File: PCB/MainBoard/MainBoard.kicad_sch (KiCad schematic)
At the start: 2 parts, among them J1 USB_C_Receptacle_USB2.0_14P

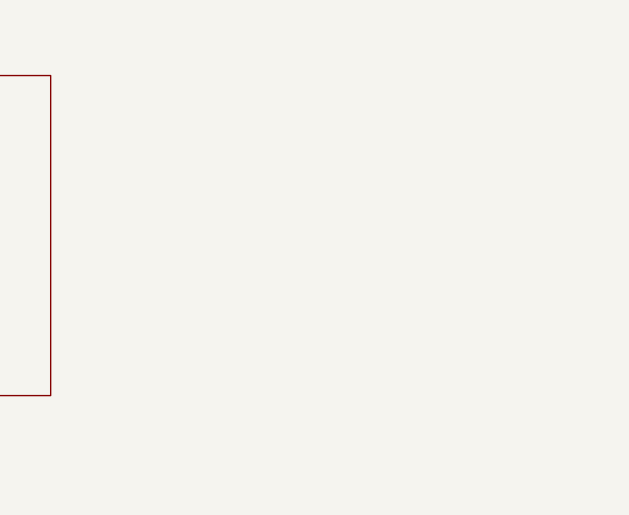
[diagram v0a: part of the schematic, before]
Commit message: Added IMU (just copied it tho...)
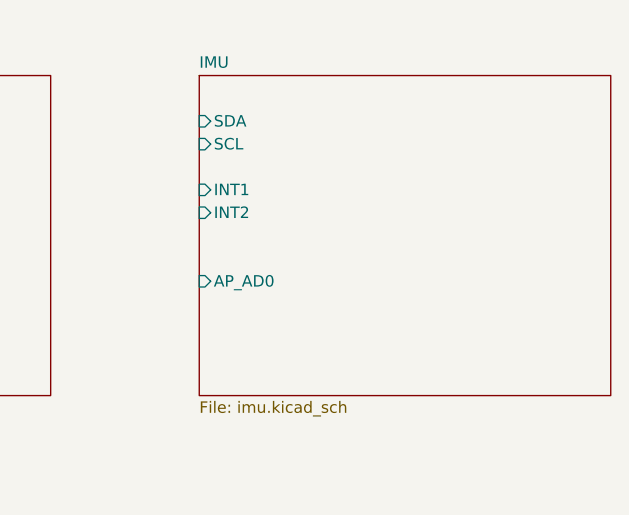
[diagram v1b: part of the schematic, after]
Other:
- added sheet IMU (imu.kicad_sch)
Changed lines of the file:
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@@
+	)
+	(sheet
+		(at 125.73 50.8)
+		(size 45.72 35.56)
+		(fields_autoplaced yes)
+		(stroke
+			(width 0.1524)
+			(type solid)
+		)
+		(fill
+			(color 0 0 0 0.0000)
+		)
+		(property "Sheetname" "IMU"
+			(at 125.73 50.0884 0)
+			(effects
+				(font
+					(size 1.27 1.27)
+				)
+				(justify left bottom)
+			)
+		)
+		(property "Sheetfile" "imu.kicad_sch"
+			(at 125.73 86.9446 0)
+			(effects
+				(font
+					(size 1.27 1.27)
+				)
+				(justify left top)
+			)
+		)
+		(pin "SDA" input
+			(at 125.73 55.88 180)
+			(effects
+				(font
+					(size 1.27 1.27)
+				)
+				(justify left)
+			)
+		)
+		(pin "SCL" input
+			(at 125.73 58.42 180)
+			(effects
+				(font
+					(size 1.27 1.27)
+				)
+				(justify left)
+			)
+		)
+		(pin "INT1" input
+			(at 125.73 63.5 180)
+			(effects
+				(font
+					(size 1.27 1.27)
+				)
+				(justify left)
+			)
+		)
+		(pin "AP_AD0" input
+			(at 125.73 73.66 180)
+			(effects
+				(font
+					(size 1.27 1.27)
+				)
+				(justify left)
+			)
+		)
+		(pin "INT2" input
+			(at 125.73 66.04 180)
+			(effects
+				(font
+					(size 1.27 1.27)
+				)
+				(justify left)
+			)
+		)
+		(instances
+			(project "MainBoard"
+				(path "/4b463b93-bd96-4cf6-bfe2-9d8869b16347"
+					(page "3")
+				)
+			)
+		)
 	)
 	(sheet

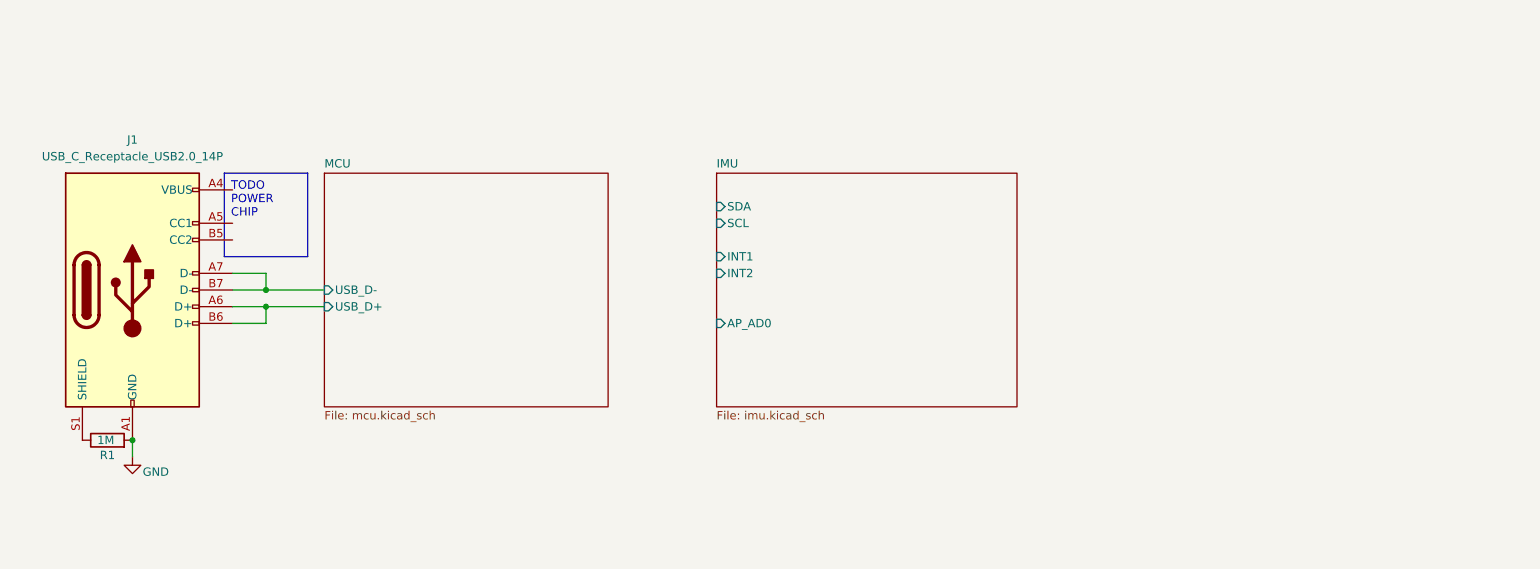
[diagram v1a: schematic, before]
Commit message: Repaired IMU and ESP symbols and footprints
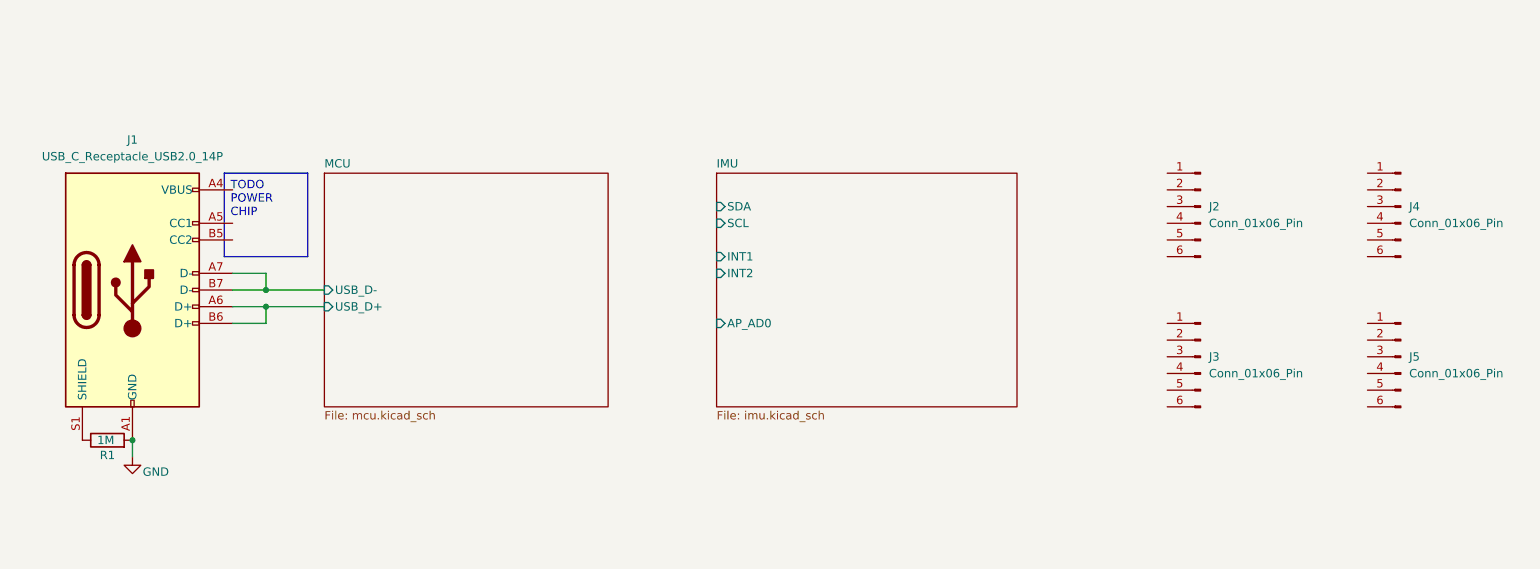
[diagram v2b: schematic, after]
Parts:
- added J2, J3, J4, J5: Conn_01x06_Pin, Connector_JST:JST_PH_B6B-PH-K_1x06_P2.00mm_Vertical, symbol Connector:Conn_01x06_Pin
- J1: footprint (none) -> Connector_USB:USB_C_Receptacle_HCTL_HC-TYPE-C-16P-01A
- R1: footprint (none) -> Resistor_SMD:R_0402_1005Metric_Pad0.72x0.64mm_HandSolder

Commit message: Added Buck converter
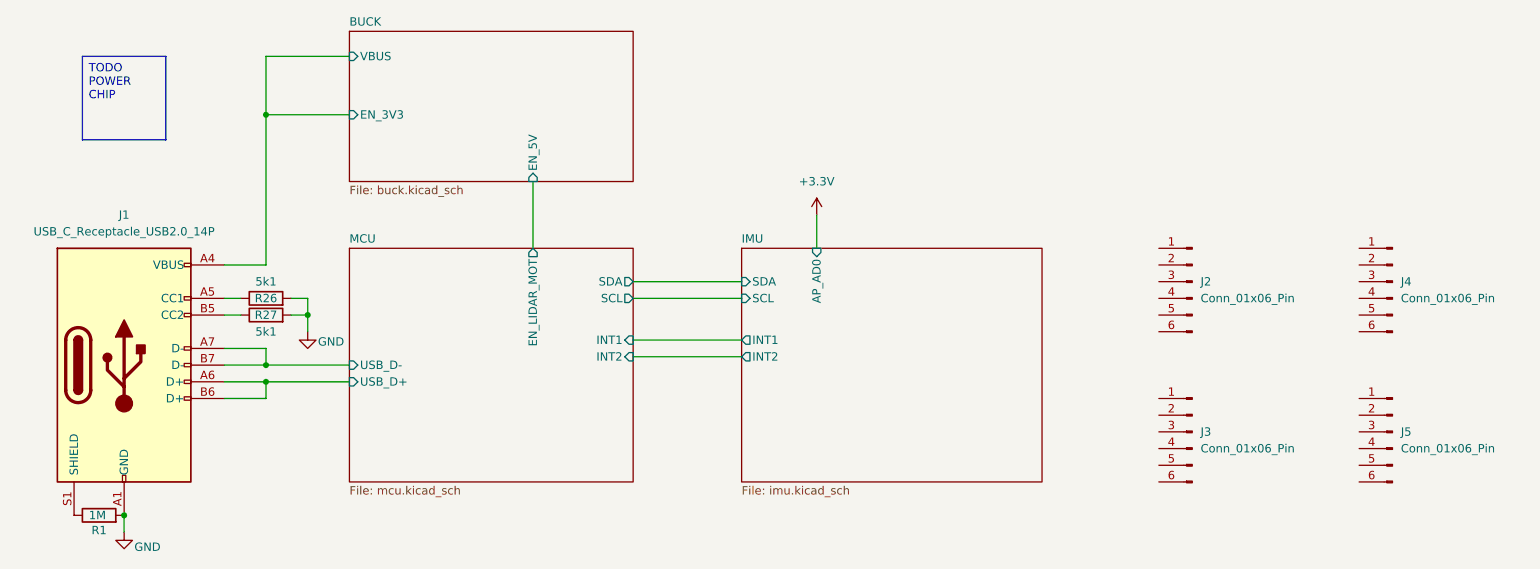
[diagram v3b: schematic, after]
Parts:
- added R26, R27: 5k1, Resistor_SMD:R_0402_1005Metric, symbol Device:R
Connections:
- net GND: now also R26.2, R27.2
- net BUCK/EN_3V3: now reaches J1.A4 (VBUS), J1.A9 (VBUS), J1.B4 (VBUS), J1.B9 (VBUS)
- net at J1.A5 (CC1): now also R26.1
- net at J1.B5 (CC2): now also R27.1
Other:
- added sheet BUCK (buck.kicad_sch)
- sheet MCU ports: added EN_LIDAR_MOT, INT1, INT2, SCL, SDA; removed none
- moved on the sheet: J1, J2, J3, J4, J5, R1
